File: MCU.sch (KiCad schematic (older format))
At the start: 14 parts, among them Y1 Crystal_8MHz_18pf

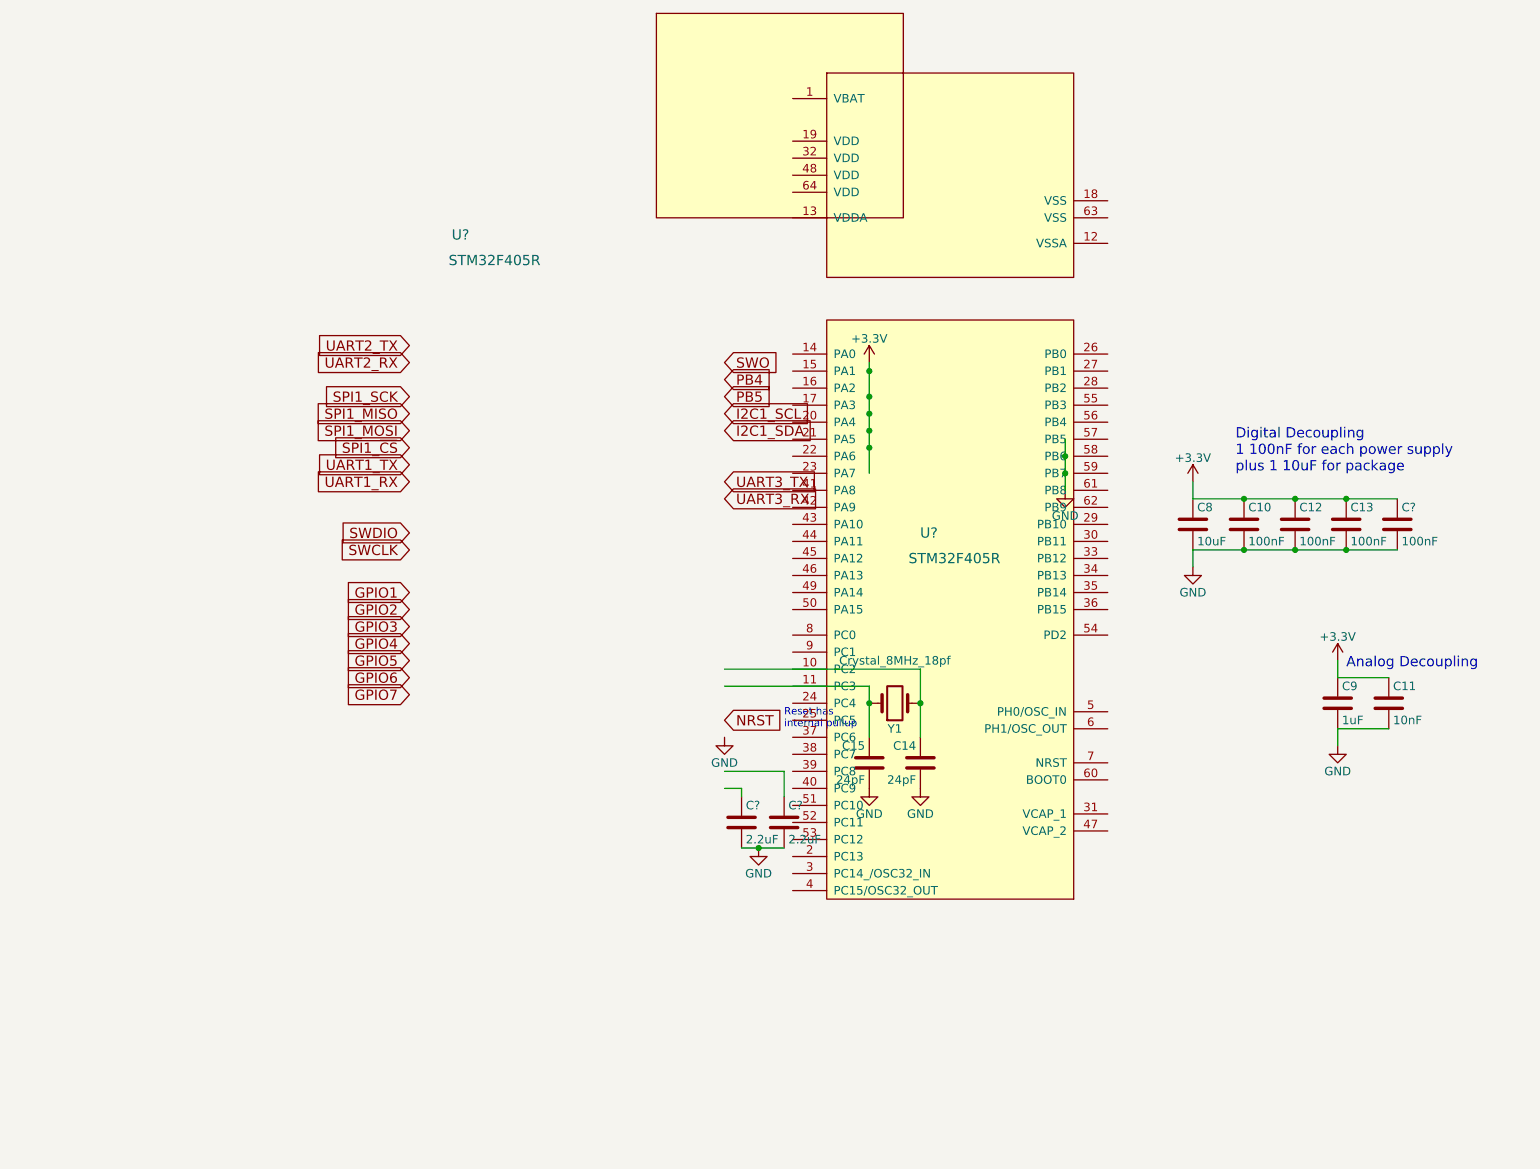
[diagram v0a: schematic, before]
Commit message: Completed schematic, Digikey parts added. 4 layer routing started.
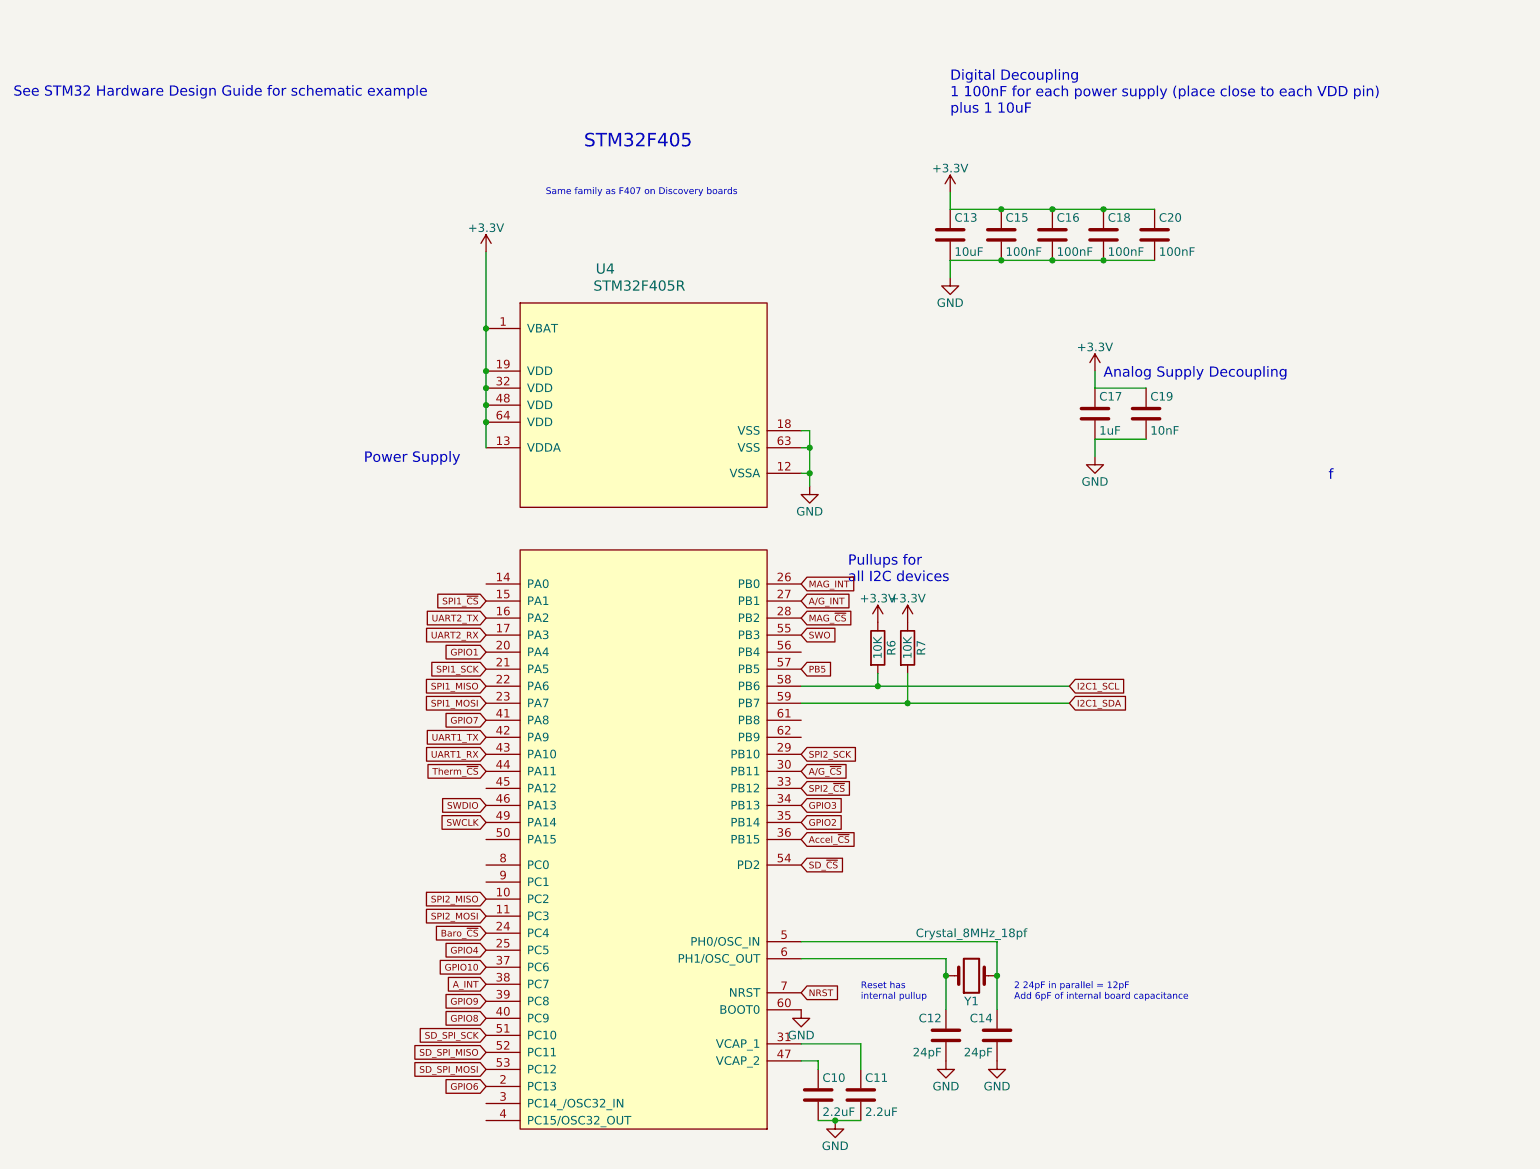
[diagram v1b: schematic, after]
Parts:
- removed U? (x2): STM32F405R, symbol STM32F405R
- added R6, R7: 10K, Resistor_SMD:R_0603_1608Metric, symbol R
- added U4: STM32F405R, Package_QFP:LQFP-64_10x10mm_P0.5mm, symbol STM32F405R
- C10, C11, C20: renamed from C?; footprint Capacitors_SMD:C_0603_HandSoldering -> Capacitor_SMD:C_0603_1608Metric
- C12: renamed from C15; footprint Capacitors_SMD:C_0603_HandSoldering -> Capacitor_SMD:C_0603_1608Metric
- C13: renamed from C8; footprint Capacitors_SMD:C_0603_HandSoldering -> Capacitor_SMD:C_0603_1608Metric
- C14: footprint Capacitors_SMD:C_0603_HandSoldering -> Capacitor_SMD:C_0603_1608Metric
- C15: renamed from C10; footprint Capacitors_SMD:C_0603_HandSoldering -> Capacitor_SMD:C_0603_1608Metric
- C16: renamed from C12; footprint Capacitors_SMD:C_0603_HandSoldering -> Capacitor_SMD:C_0603_1608Metric
- C17: renamed from C9; footprint Capacitors_SMD:C_0603_HandSoldering -> Capacitor_SMD:C_0603_1608Metric
- C18: renamed from C13; footprint Capacitors_SMD:C_0603_HandSoldering -> Capacitor_SMD:C_0603_1608Metric
- C19: renamed from C11; footprint Capacitors_SMD:C_0603_HandSoldering -> Capacitor_SMD:C_0603_1608Metric
- Y1: footprint Crystals:Crystal_SMD_SeikoEpson_MA505-2pin_12.7x5.1mm -> Crystal:Crystal_SMD_SeikoEpson_MA505-2Pin_12.7x5.1mm; Digikey (none) -> 535-9089-1-ND
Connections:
- net labels added: A/G_INT, A/G_~CS, A_INT, Accel_~CS, Baro_~CS, GPIO10, GPIO8, GPIO9, MAG_INT, MAG_~CS, SD_SPI_MISO, SD_SPI_MOSI, SD_SPI_SCK, SD_~CS, SPI2_MISO, SPI2_MOSI, SPI2_SCK, SPI2_~CS, Therm_~CS
- net labels removed: GPIO5, PB4, UART3_RX, UART3_TX
- wire segments 21 -> 27
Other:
- note added: "2 24pF in parallel = 12pF\nAdd 6pF of internal board capacitance"
- note added: "Analog Supply Decoupling"
- note added: "Digital Decoupling\n1 100nF for each power supply (place close to each VDD pin)\nplus 1 10uF"
- note added: "Power Supply"
- note added: "Pullups for\nall I2C devices\n"
- note added: "STM32F405"
- note added: "Same family as F407 on Discovery boards"
- note added: "See STM32 Hardware Design Guide for schematic example\n"
- note added: "f"
- note removed: "Analog Decoupling"
- note removed: "Digital Decoupling\n1 100nF for each power supply\nplus 1 10uF for package"
- moved on the sheet: C10, C11, C12, C13, C14, C15, C16, C17, C18, C19, C20, Y1
